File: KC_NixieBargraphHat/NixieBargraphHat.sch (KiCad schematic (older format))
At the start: 13 parts

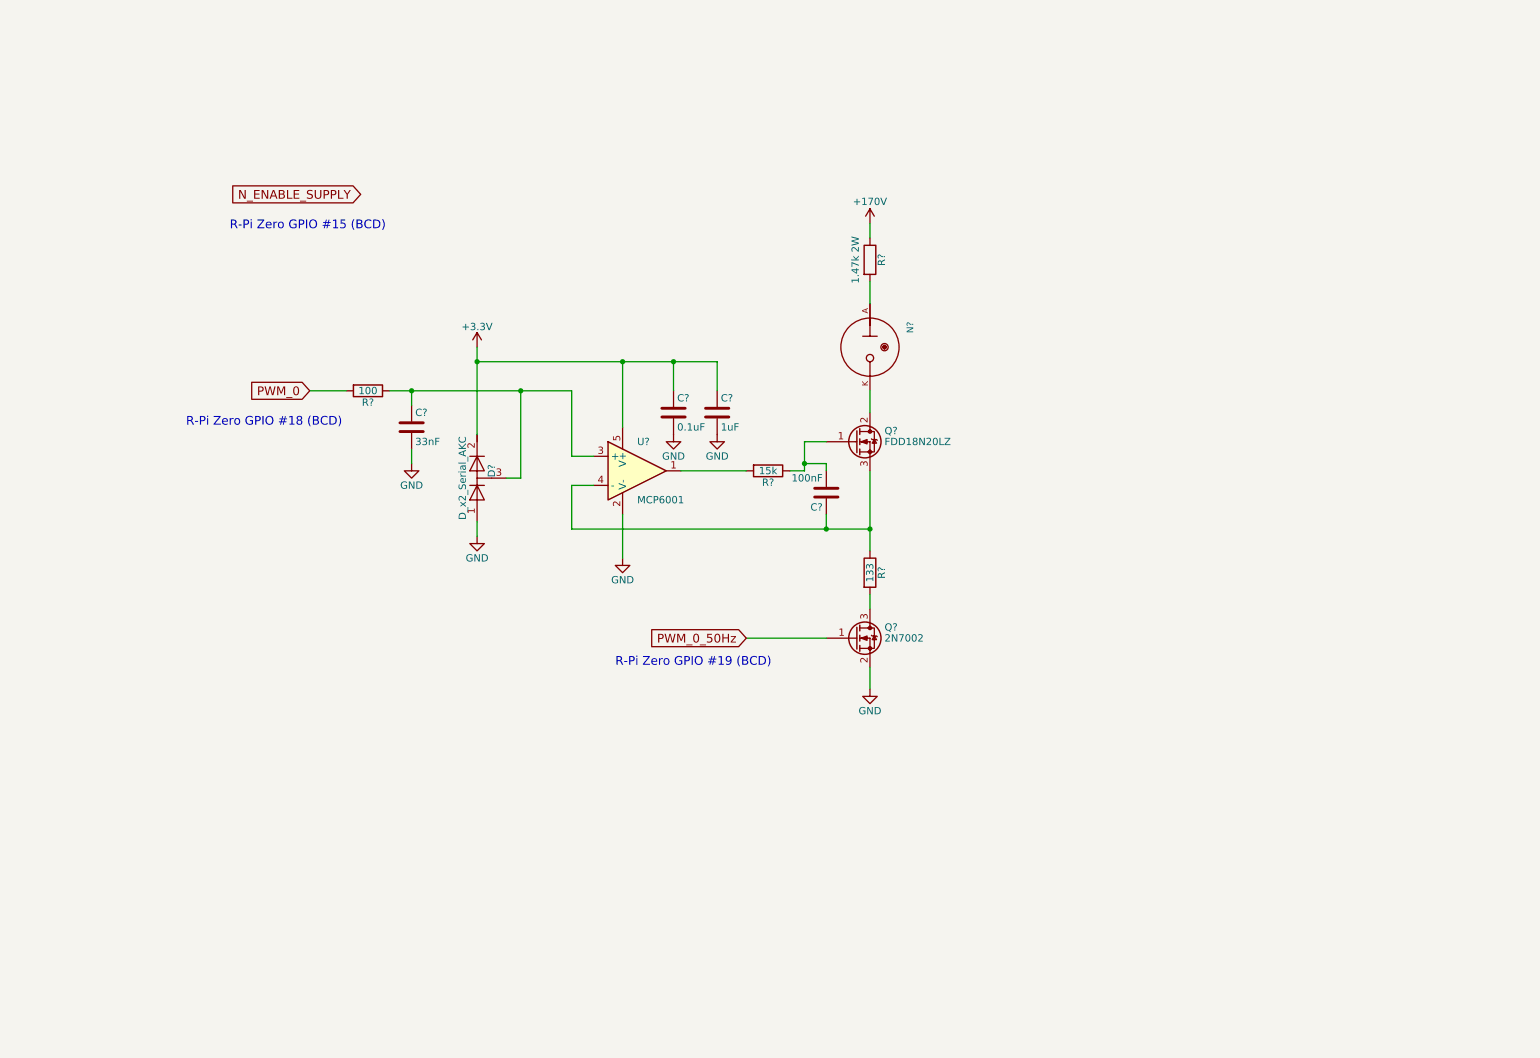
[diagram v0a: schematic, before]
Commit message: Added connectors for the power supply and the Raspberry Pi header
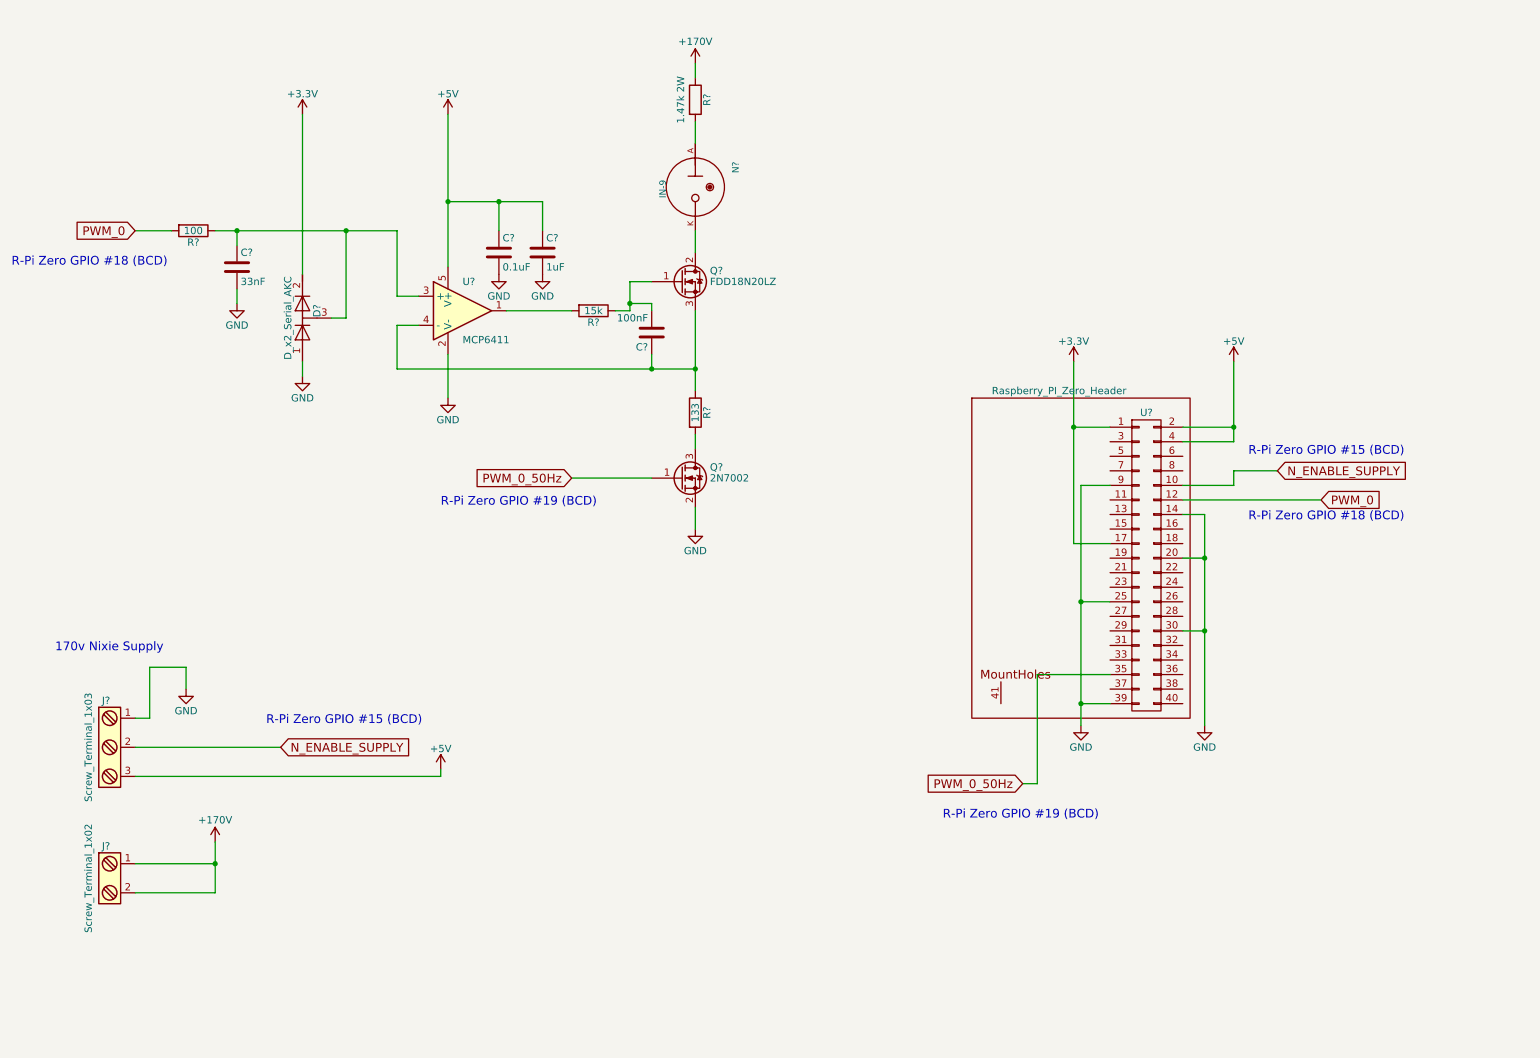
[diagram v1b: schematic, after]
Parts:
- added J?: Screw_Terminal_1x03, symbol Screw_Terminal_1x03
- added J?: Screw_Terminal_1x02, symbol Screw_Terminal_1x02
- added U?: Raspberry_PI_Zero_Header, symbol Raspberry_PI_Zero_Hat
- U?: value MCP6001 -> MCP6411
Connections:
- net +170V: now also J?.1, J?.2
- net +3V3: now also U?.1 (P1), U?.17 (P17); no longer C?.1, C?.1, U?.5 (V+)
- net GND: now also J?.1, U?.14 (P14), U?.20 (P20), U?.25 (P25), U?.30 (P30), U?.39 (P39), U?.9 (P9)
- net N_ENABLE_SUPPLY: now also J?.2, U?.10 (P10)
- net PWM_0: now also U?.12 (P12)
- net PWM_0_50Hz: now also U?.35 (P35)
- new net +5V: C?.1, C?.1, J?.3, U?.2 (P2), U?.4 (P4), U?.5 (V+)
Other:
- note added: "170v Nixie Supply \n"
- moved on the sheet: C?, D?, N?, Q?, R?, U?

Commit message: removed image
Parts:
- gave numbers to parts that had none: 16
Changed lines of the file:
@@
 PWM_0
 $Comp
-L R R?
+L R R1
 U 1 1 5BCD535B
 P 2200 2100
-F 0 "R?" V 2280 2100 50  0000 C CNN
+F 0 "R1" V 2280 2100 50  0000 C CNN
 F 1 "100" V 2200 2100 50  0000 C CNN
 F 2 "" V 2130 2100 50  0001 C CNN
@@
 $EndComp
 $Comp
-L C C?
+L C C1
 U 1 1 5BCD538A
 P 2500 2350
-F 0 "C?" H 2525 2450 50  0000 L CNN
+F 0 "C1" H 2525 2450 50  0000 L CNN
 F 1 "33nF" H 2525 2250 50  0000 L CNN
 F 2 "" H 2538 2200 50  0001 C CNN
@@
 $EndComp
 $Comp
-L R R?
+L R R4
 U 1 1 5BCD53AB
 P 5650 3350
-F 0 "R?" V 5730 3350 50  0000 C CNN
+F 0 "R4" V 5730 3350 50  0000 C CNN
 F 1 "133" V 5650 3350 50  0000 C CNN
 F 2 "" V 5580 3350 50  0001 C CNN
@@
 $EndComp
 $Comp
-L R R?
+L R R2
 U 1 1 5BCD5438
 P 4950 2650
-F 0 "R?" V 5030 2650 50  0000 C CNN
+F 0 "R2" V 5030 2650 50  0000 C CNN
 F 1 "15k" V 4950 2650 50  0000 C CNN
 F 2 "" V 4880 2650 50  0001 C CNN
@@
 $EndComp
 $Comp
-L R R?
+L R R3
 U 1 1 5BCD54E5
 P 5650 1200
-F 0 "R?" V 5730 1200 50  0000 C CNN
+F 0 "R3" V 5730 1200 50  0000 C CNN
 F 1 "1.47k 2W" V 5550 1200 50  0000 C CNN
 F 2 "" V 5580 1200 50  0001 C CNN
@@
 $EndComp
 $Comp
-L 2N7002 Q?
+L 2N7002 Q2
 U 1 1 5BCD5617
 P 5550 3800
-F 0 "Q?" H 5750 3875 50  0000 L CNN
+F 0 "Q2" H 5750 3875 50  0000 L CNN
 F 1 "2N7002" H 5750 3800 50  0000 L CNN
 F 2 "TO_SOT_Packages_SMD:SOT-23" H 5750 3725 50  0001 L CIN
@@
 $EndComp
 $Comp
-L C C?
+L C C4
 U 1 1 5BCD5690
 P 5350 2800
-F 0 "C?" H 5375 2900 50  0000 L CNN
+F 0 "C4" H 5375 2900 50  0000 L CNN
 F 1 "100nF" H 5375 2700 50  0000 L CNN
 F 2 "" H 5388 2650 50  0001 C CNN
@@
 $EndComp
 $Comp
-L BSP129 Q?
+L BSP129 Q1
 U 1 1 5C200374
 P 5550 2450
-F 0 "Q?" H 5750 2525 50  0000 L CNN
+F 0 "Q1" H 5750 2525 50  0000 L CNN
 F 1 "FDD18N20LZ" H 5750 2450 50  0000 L CNN
 F 2 "TO_SOT_Packages_SMD:SOT-223-3Lead_TabPin2" H 5750 2375 50  0001 L CIN
@@
 $EndComp
 $Comp
-L MCP6001 U?
+L MCP6001 U1
 U 1 1 5BCD55A3
 P 4050 2650
-F 0 "U?" H 4050 2850 50  0000 L CNN
+F 0 "U1" H 4050 2850 50  0000 L CNN
 F 1 "MCP6411" H 4050 2450 50  0000 L CNN
 F 2 "" H 4050 2650 50  0001 C CNN
@@
 $EndComp
 $Comp
-L GND #PWR?
+L GND #PWR12
 U 1 1 5C200954
 P 5650 4150
-F 0 "#PWR?" H 5650 3900 50  0001 C CNN
+F 0 "#PWR12" H 5650 3900 50  0001 C CNN
 F 1 "GND" H 5650 4000 50  0000 C CNN
 F 2 "" H 5650 4150 50  0001 C CNN
@@
 $EndComp
 $Comp
-L GND #PWR?
+L GND #PWR8
 U 1 1 5C200983
 P 3950 3250
-F 0 "#PWR?" H 3950 3000 50  0001 C CNN
+F 0 "#PWR8" H 3950 3000 50  0001 C CNN
 F 1 "GND" H 3950 3100 50  0000 C CNN
 F 2 "" H 3950 3250 50  0001 C CNN
@@
 $EndComp
 $Comp
-L GND #PWR?
+L GND #PWR3
 U 1 1 5C2009B2
 P 2500 2600
-F 0 "#PWR?" H 2500 2350 50  0001 C CNN
+F 0 "#PWR3" H 2500 2350 50  0001 C CNN
 F 1 "GND" H 2500 2450 50  0000 C CNN
 F 2 "" H 2500 2600 50  0001 C CNN
@@
 PWM_0_50Hz
 $Comp
-L +170V #PWR?
+L +170V #PWR11
 U 1 1 5C201CD2
 P 5650 950
-F 0 "#PWR?" H 5650 800 50  0001 C CNN
+F 0 "#PWR11" H 5650 800 50  0001 C CNN
 F 1 "+170V" H 5650 1100 50  0000 C CNN
 F 2 "" H 5900 1000 50  0001 C CNN
@@
 $EndComp
 $Comp
-L IN-9 N?
+L IN-9 N1
 U 1 1 5C2015AE
 P 5650 1800
-F 0 "N?" H 5475 2050 45  0000 L BNN
+F 0 "N1" H 5475 2050 45  0000 L BNN
 F 1 "IN-9" H 5600 1550 45  0000 L BNN
 F 2 "nixies-us_IN-9" H 5680 1950 20  0001 C CNN
@@
 $EndComp
 $Comp
-L GND #PWR?
+L GND #PWR5
 U 1 1 5C202930
 P 2950 3100
-F 0 "#PWR?" H 2950 2850 50  0001 C CNN
+F 0 "#PWR5" H 2950 2850 50  0001 C CNN
 F 1 "GND" H 2950 2950 50  0000 C CNN
 F 2 "" H 2950 3100 50  0001 C CNN
@@
 $EndComp
 $Comp
-L +3.3V #PWR?
+L +3.3V #PWR4
 U 1 1 5C202953
 P 2950 1300
-F 0 "#PWR?" H 2950 1150 50  0001 C CNN
+F 0 "#PWR4" H 2950 1150 50  0001 C CNN
 F 1 "+3.3V" H 2950 1440 50  0000 C CNN
 F 2 "" H 2950 1300 50  0001 C CNN
@@
 R-Pi Zero GPIO #18 (BCD)
 $Comp
-L D_x2_Serial_AKC D?
+L D_x2_Serial_AKC D1
 U 1 1 5C202BDD
 P 2950 2700
-F 0 "D?" H 3000 2600 50  0000 C CNN
+F 0 "D1" H 3000 2600 50  0000 C CNN
 F 1 "D_x2_Serial_AKC" H 2950 2800 50  0000 C CNN
 F 2 "" H 2950 2700 50  0001 C CNN
@@
 Connection ~ 5350 3050
 $Comp
-L C C?
+L C C2
 U 1 1 5C31D287
 P 4300 2250
-F 0 "C?" H 4325 2350 50  0000 L CNN
+F 0 "C2" H 4325 2350 50  0000 L CNN
 F 1 "0.1uF" H 4325 2150 50  0000 L CNN
 F 2 "" H 4338 2100 50  0001 C CNN
@@
 	4300 1900 4300 2100
 $Comp
-L GND #PWR?
+L GND #PWR9
 U 1 1 5C31D35E
 P 4300 2400
-F 0 "#PWR?" H 4300 2150 50  0001 C CNN
+F 0 "#PWR9" H 4300 2150 50  0001 C CNN
 F 1 "GND" H 4300 2250 50  0000 C CNN
 F 2 "" H 4300 2400 50  0001 C CNN
@@
 $EndComp
 $Comp
-L C C?
+L C C3
 U 1 1 5C31D3ED
 P 4600 2250
-F 0 "C?" H 4625 2350 50  0000 L CNN
+F 0 "C3" H 4625 2350 50  0000 L CNN
 F 1 "1uF" H 4625 2150 50  0000 L CNN
 F 2 "" H 4638 2100 50  0001 C CNN
@@
 $EndComp
 $Comp
-L GND #PWR?
+L GND #PWR10
 U 1 1 5C31D47B
 P 4600 2400
-F 0 "#PWR?" H 4600 2150 50  0001 C CNN
+F 0 "#PWR10" H 4600 2150 50  0001 C CNN
 F 1 "GND" H 4600 2250 50  0000 C CNN
 F 2 "" H 4600 2400 50  0001 C CNN
@@
 R-Pi Zero GPIO #15 (BCD)\n
 $Comp
-L Raspberry_PI_Zero_Hat U?
+L Raspberry_PI_Zero_Hat U2
 U 1 1 5C3AAF08
 P 8350 4300
-F 0 "U?" H 8750 5250 50  0000 C CNN
+F 0 "U2" H 8750 5250 50  0000 C CNN
 F 1 "Raspberry_PI_Zero_Header" H 8150 5400 50  0000 C CNN
 F 2 "" H 8750 3200 50  0000 C CNN
@@
 $EndComp
 $Comp
-L Screw_Terminal_1x03 J?
+L Screw_Terminal_1x03 J1
 U 1 1 5C3AC45A
 P 1600 5650
-F 0 "J?" H 1600 6000 50  0000 C TNN
+F 0 "J1" H 1600 6000 50  0000 C TNN
 F 1 "Screw_Terminal_1x03" V 1450 5650 50  0000 C TNN
 F 2 "" H 1600 5325 50  0001 C CNN
@@
 $EndComp
 $Comp
-L Screw_Terminal_1x02 J?
+L Screw_Terminal_1x02 J2
 U 1 1 5C3AC534
 P 1600 6550
-F 0 "J?" H 1600 6800 50  0000 C TNN
+F 0 "J2" H 1600 6800 50  0000 C TNN
 F 1 "Screw_Terminal_1x02" V 1450 6550 50  0000 C TNN
 F 2 "" H 1600 6325 50  0001 C CNN
@@
 $EndComp
 $Comp
-L +170V #PWR?
+L +170V #PWR2
 U 1 1 5C3ACB34
 P 2350 6300
-F 0 "#PWR?" H 2350 6150 50  0001 C CNN
+F 0 "#PWR2" H 2350 6150 50  0001 C CNN
 F 1 "+170V" H 2350 6450 50  0000 C CNN
 F 2 "" H 2600 6350 50  0001 C CNN
@@
 Connection ~ 2350 6450
 $Comp
-L GND #PWR?
+L GND #PWR1
 U 1 1 5C3ACCC6
 P 2150 5250
-F 0 "#PWR?" H 2150 5000 50  0001 C CNN
+F 0 "#PWR1" H 2150 5000 50  0001 C CNN
 F 1 "GND" H 2150 5100 50  0000 C CNN
 F 2 "" H 2150 5250 50  0001 C CNN
@@
 	2800 5650 1800 5650
 $Comp
-L +5V #PWR?
+L +5V #PWR6
 U 1 1 5C3ACE7B
 P 3900 5800
-F 0 "#PWR?" H 3900 5650 50  0001 C CNN
+F 0 "#PWR6" H 3900 5650 50  0001 C CNN
 F 1 "+5V" H 3900 5940 50  0000 C CNN
 F 2 "" H 3900 5800 50  0001 C CNN
@@
 Connection ~ 9150 4350
 $Comp
-L GND #PWR?
+L GND #PWR14
 U 1 1 5C3AD39F
 P 8300 5500
-F 0 "#PWR?" H 8300 5250 50  0001 C CNN
+F 0 "#PWR14" H 8300 5250 50  0001 C CNN
 F 1 "GND" H 8300 5350 50  0000 C CNN
 F 2 "" H 8300 5500 50  0001 C CNN
@@
 Connection ~ 8300 4650
 $Comp
-L +5V #PWR?
+L +5V #PWR16
 U 1 1 5C3AD553
 P 9350 3000
-F 0 "#PWR?" H 9350 2850 50  0001 C CNN
+F 0 "#PWR16" H 9350 2850 50  0001 C CNN
 F 1 "+5V" H 9350 3140 50  0000 C CNN
 F 2 "" H 9350 3000 50  0001 C CNN
@@
 Connection ~ 9350 3450
 $Comp
-L +3.3V #PWR?
+L +3.3V #PWR13
 U 1 1 5C3AD63C
 P 8250 3000
-F 0 "#PWR?" H 8250 2850 50  0001 C CNN
+F 0 "#PWR13" H 8250 2850 50  0001 C CNN
 F 1 "+3.3V" H 8250 3140 50  0000 C CNN
 F 2 "" H 8250 3000 50  0001 C CNN
@@
 Connection ~ 8250 3450
 $Comp
-L GND #PWR?
+L GND #PWR15
 U 1 1 5C3AD83D
 P 9150 5500
-F 0 "#PWR?" H 9150 5250 50  0001 C CNN
+F 0 "#PWR15" H 9150 5250 50  0001 C CNN
 F 1 "GND" H 9150 5350 50  0000 C CNN
 F 2 "" H 9150 5500 50  0001 C CNN
@@
 	4300 1900 4600 1900
 $Comp
-L +5V #PWR?
+L +5V #PWR7
 U 1 1 5C3ADB25
 P 3950 1300
-F 0 "#PWR?" H 3950 1150 50  0001 C CNN
+F 0 "#PWR7" H 3950 1150 50  0001 C CNN
 F 1 "+5V" H 3950 1440 50  0000 C CNN
 F 2 "" H 3950 1300 50  0001 C CNN
